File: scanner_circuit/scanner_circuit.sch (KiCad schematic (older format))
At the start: 11 parts

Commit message: Added buttons on Kicad
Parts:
- added BlueButton, GreenButton, RedButton: SW_Push_Open_Dual, symbol Switch:SW_Push_Open_Dual
- added R?: 68k, symbol Device:R
- added R? (x2): 20k, symbol Device:R
- added R?: 10k, symbol Device:R
- added R?: 100k, symbol Device:R
- added U?: dragino_lora_shield, symbol scanner_components:dragino_lora_shield
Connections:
- wire segments 41 -> 59
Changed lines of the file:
@@
-$EndComp
-$Comp
-L scanner_components:FGPMMOPA6H(gps) MOD?
-U 1 1 5DE0B476
-P 6500 3850
-F 0 "MOD?" H 6778 3896 50  0000 L CNN
-F 1 "FGPMMOPA6H(gps)" H 6778 3805 50  0000 L CNN
-F 2 "" H 6500 3950 50  0001 C CNN
-F 3 "" H 6500 3950 50  0001 C CNN
-	1    6500 3850
-	1    0    0    -1
 $EndComp
 $Comp
@@
 $EndComp
 Wire Wire Line
-	5300 3650 5900 3650
-Wire Wire Line
-	5900 3550 5300 3550
-Wire Wire Line
 	5300 3550 5300 3500
 $Comp
@@
 Wire Wire Line
 	5300 4250 5900 4250
+Wire Wire Line
+	5300 3650 5900 3650
+Wire Wire Line
+	5900 3550 5300 3550
+$Comp
+L scanner_components:FGPMMOPA6H(gps) MOD?
+U 1 1 5DE0B476
+P 6500 3850
+F 0 "MOD?" H 6778 3896 50  0000 L CNN
+F 1 "FGPMMOPA6H(gps)" H 6778 3805 50  0000 L CNN
+F 2 "" H 6500 3950 50  0001 C CNN
+F 3 "" H 6500 3950 50  0001 C CNN
+	1    6500 3850
+	1    0    0    -1
+$EndComp
+Wire Wire Line
+	8000 1950 8000 2200
+$Comp
+L power:GND #PWR?
+U 1 1 5DEF5DF5
+P 8000 2200
+F 0 "#PWR?" H 8000 1950 50  0001 C CNN
+F 1 "GND" H 8000 2050 50  0000 C CNN
+F 2 "" H 8000 2200 50  0001 C CNN
+F 3 "" H 8000 2200 50  0001 C CNN
+	1    8000 2200
+	1    0    0    -1
+$EndComp
+$Comp
+L power:+5VP #PWR?
+U 1 1 5DEFC89F
+P 7800 2200
+F 0 "#PWR?" H 7800 2050 50  0001 C CNN
+F 1 "+5VP" H 7815 2373 50  0000 C CNN
+F 2 "" H 7800 2200 50  0001 C CNN
+F 3 "" H 7800 2200 50  0001 C CNN
+	1    7800 2200
+	-1   0    0    1
+$EndComp
+Wire Wire Line
+	7800 2200 7800 1950
+$Comp
+L Device:R R?
+U 1 1 5DF037F4
+P 9800 3300
+F 0 "R?" V 9593 3300 50  0000 C CNN
+F 1 "68k" V 9684 3300 50  0000 C CNN
+F 2 "" V 9730 3300 50  0001 C CNN
+F 3 "~" H 9800 3300 50  0001 C CNN
+	1    9800 3300
+	0    1    1    0
+$EndComp
+$Comp
+L Switch:SW_Push_Open_Dual RedButton
+U 1 1 5DF02678
+P 10600 3300
+F 0 "RedButton" H 10600 3510 50  0000 C CNN
+F 1 "SW_Push_Open_Dual" H 10600 3419 50  0000 C CNN
+F 2 "" H 10600 3500 50  0001 C CNN
+F 3 "~" H 10600 3500 50  0001 C CNN
+	1    10600 3300
+	1    0    0    -1
+$EndComp
+Wire Wire Line
+	9950 3300 10400 3300
+$Comp
+L power:+5VP #PWR?
+U 1 1 5DF07955
+P 9450 3300
+F 0 "#PWR?" H 9450 3150 50  0001 C CNN
+F 1 "+5VP" H 9465 3473 50  0000 C CNN
+F 2 "" H 9450 3300 50  0001 C CNN
+F 3 "" H 9450 3300 50  0001 C CNN
+	1    9450 3300
+	0    -1   -1   0
+$EndComp
+Wire Wire Line
+	9450 3300 9650 3300
+$Comp
+L Device:R R?
+U 1 1 5DF0A509
+P 9800 4150
+F 0 "R?" V 9593 4150 50  0000 C CNN
+F 1 "20k" V 9684 4150 50  0000 C CNN
+F 2 "" V 9730 4150 50  0001 C CNN
+F 3 "~" H 9800 4150 50  0001 C CNN
+	1    9800 4150
+	0    1    1    0
+$EndComp
+$Comp
+L Switch:SW_Push_Open_Dual BlueButton
+U 1 1 5DF0A50F
+P 10600 4150
+F 0 "BlueButton" H 10600 4360 50  0000 C CNN
+F 1 "SW_Push_Open_Dual" H 10600 4269 50  0000 C CNN
+F 2 "" H 10600 4350 50  0001 C CNN
+F 3 "~" H 10600 4350 50  0001 C CNN
+	1    10600 4150
+	1    0    0    -1
+$EndComp
+Wire Wire Line
+	9950 4150 10400 4150
+$Comp
+L power:+5VP #PWR?
+U 1 1 5DF0A516
+P 9450 4150
+F 0 "#PWR?" H 9450 4000 50  0001 C CNN
+F 1 "+5VP" H 9465 4323 50  0000 C CNN
+F 2 "" H 9450 4150 50  0001 C CNN
+F 3 "" H 9450 4150 50  0001 C CNN
+	1    9450 4150
+	0    -1   -1   0
+$EndComp
+Wire Wire Line
+	9450 4150 9650 4150
+$Comp
+L Device:R R?
+U 1 1 5DF0D043
+P 9450 5000
+F 0 "R?" V 9243 5000 50  0000 C CNN
+F 1 "10k" V 9334 5000 50  0000 C CNN
+F 2 "" V 9380 5000 50  0001 C CNN
+F 3 "~" H 9450 5000 50  0001 C CNN
+	1    9450 5000
+	0    1    1    0
+$EndComp
+$Comp
+L Switch:SW_Push_Open_Dual GreenButton
+U 1 1 5DF0D049
+P 10600 5000
+F 0 "GreenButton" H 10600 5210 50  0000 C CNN
+F 1 "SW_Push_Open_Dual" H 10600 5119 50  0000 C CNN
+F 2 "" H 10600 5200 50  0001 C CNN
+F 3 "~" H 10600 5200 50  0001 C CNN
+	1    10600 5000
+	1    0    0    -1
+$EndComp
+$Comp
+L power:+5VP #PWR?
+U 1 1 5DF0D050
+P 9100 5000
+F 0 "#PWR?" H 9100 4850 50  0001 C CNN
+F 1 "+5VP" H 9115 5173 50  0000 C CNN
+F 2 "" H 9100 5000 50  0001 C CNN
+F 3 "" H 9100 5000 50  0001 C CNN
+	1    9100 5000
+	0    -1   -1   0
+$EndComp
+Wire Wire Line
+	9100 5000 9300 5000
+$Comp
+L scanner_components:dragino_lora_shield U?
+U 1 1 5DEF3113
+P 7000 2100
+F 0 "U?" H 8878 2771 50  0000 L CNN
+F 1 "dragino_lora_shield" H 8878 2680 50  0000 L CNN
+F 2 "" H 7000 2850 50  0001 C CNN
+F 3 "" H 7000 2850 50  0001 C CNN
+	1    7000 2100
+	1    0    0    -1
+$EndComp
+Wire Wire Line
+	8700 1950 8700 2650
+Wire Wire Line
+	8700 3500 10400 3500
+Wire Wire Line
+	10400 4350 8700 4350
+Wire Wire Line
+	8700 4350 8700 3500
+Connection ~ 8700 3500
+Wire Wire Line
+	10400 5200 8700 5200
+Wire Wire Line
+	8700 5200 8700 4350
+Connection ~ 8700 4350
+Wire Wire Line
+	8700 2650 9100 2650
+Connection ~ 8700 2650
+Wire Wire Line
+	8700 2650 8700 3500
+$Comp
+L Device:R R?
+U 1 1 5DF1893C
+P 9250 2650
+F 0 "R?" V 9043 2650 50  0000 C CNN
+F 1 "100k" V 9134 2650 50  0000 C CNN
+F 2 "" V 9180 2650 50  0001 C CNN
+F 3 "~" H 9250 2650 50  0001 C CNN
+	1    9250 2650
+	0    1    1    0
+$EndComp
+Wire Wire Line
+	9400 2650 10050 2650
+$Comp
+L power:GND #PWR?
+U 1 1 5DF1B53E
+P 10050 2650
+F 0 "#PWR?" H 10050 2400 50  0001 C CNN
+F 1 "GND" H 10055 2477 50  0000 C CNN
+F 2 "" H 10050 2650 50  0001 C CNN
+F 3 "" H 10050 2650 50  0001 C CNN
+	1    10050 2650
+	0    -1   -1   0
+$EndComp
+Wire Wire Line
+	9600 5000 9800 5000
+$Comp
+L Device:R R?
+U 1 1 5DF20956
+P 9950 5000
+F 0 "R?" V 9743 5000 50  0000 C CNN
+F 1 "20k" V 9834 5000 50  0000 C CNN
+F 2 "" V 9880 5000 50  0001 C CNN
+F 3 "~" H 9950 5000 50  0001 C CNN
+	1    9950 5000
+	0    1    1    0
+$EndComp
+Wire Wire Line
+	10100 5000 10400 5000
 $EndSCHEMATC

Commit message: Working on schematic for TTN Mapper
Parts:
- removed BlueButton, GreenButton, RedButton: SW_Push_Open_Dual, symbol Switch:SW_Push_Open_Dual
- added SW?: Red_Button, symbol Switch:SW_Push
- added SW?: Blue_Button, symbol Switch:SW_Push
- added SW?: Green_Button, symbol Switch:SW_Push
- MOD?: value FGPMMOPA6H(gps) -> GPS MODUL - FGPMMOPA6H
- U?: value dragino_lora_shield -> LoRa Shield
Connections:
- net labels added: A0, A1
- wire segments 59 -> 62
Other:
- moved on the sheet: C?, MOD?, Q?, R?, U?

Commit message: Worked further on TTN mapper and fixed a bug in main file
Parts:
- added C6, C8: 100nF, symbol Device:C_Small
- added C7, C9: 10uF, symbol Device:CP_Small
- added DS1: LCD Screen, Display:WC1602A, symbol Display_Character:WC1602A
- added R10, R11, R13: 120R, symbol Device:R
- added R12: 620R, symbol Device:R
- added R4: 220R, symbol Device:R_Small
- added RV1: 10K_Potentiometer, symbol Device:R_POT
- added U3: LD1117S33TR_SOT223, Package_TO_SOT_SMD:SOT-223-3_TabPin2, symbol Regulator_Linear:LD1117S33TR_SOT223
- added U4: LM317_TO220, Package_TO_SOT_THT:TO-220-3_Vertical, symbol Regulator_Linear:LM337_TO220
- MOD1: renamed from MOD?; value GPS MODUL - FGPMMOPA6H -> GPS MODULE
- gave numbers to parts that had none: 19
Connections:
- net UNO_RX is gone; now on net D3: U1.5 (PD3)
- net +3V3: now also C7.1, U3.2 (VO)
- net +5VP: now also C9.1, DS1.2 (VDD), R10.2, R4.2, RV1.1, U4.3 (VO)
- net A1: now also U2.31 (1)
- net GND: now also U2.24 (GND), U2.25 (GND), C6.2, C7.2, C8.2, C9.2, DS1.1 (VSS), DS1.16 (LED(-)), DS1.5 (R/W), R13.1, RV1.3, U3.1 (GND)
- net D5: now reaches U1.11 (PD5)
- net D5: now also U2.6 (5), DS1.11 (D4)
- net D6: now reaches U1.12 (PD6)
- net D6: now also U2.7 (6)
- net D7: now reaches U1.13 (PD7)
- net D7: now also U2.8 (7)
- net D8: now reaches U1.14 (PB0)
- net D8: now also U2.9 (8)
- net D9: now reaches U1.15 (PB1)
- net D9: now also U2.10 (9)
- net D10: now reaches U1.16 (PB2)
- net D10: now also U2.11 (10)
- net D11: now reaches U1.17 (PB3)
- net D11: now also U2.12 (11)
- net D12: now reaches U1.18 (PB4)
- net D12: now also U2.13 (12)
- net D13: now reaches U1.19 (PB5)
- net D13: now also U2.14 (13)
- net RX: now reaches U1.2 (PD0)
- net RX: now also U2.2 (1)
- net AREF: now reaches U1.21 (AREF)
- net AREF: now also U2.16 (AREF)
- net A2: now reaches U1.25 (PC2)
- net A2: now also U2.30 (2)
- net A3: now reaches U1.26 (PC3)
- net A3: now also U2.29 (3), DS1.14 (D7)
- net A4: now reaches U1.27 (PC4)
- net A4: now also U2.17 (SDA), U2.28 (4), DS1.6 (E)
- net A5: now reaches U1.28 (PC5)
- net A5: now also U2.18 (SCL), U2.27 (5), DS1.4 (RS)
- net TX: now reaches U1.3 (PD1)
- net TX: now also U2.1 (0)
- net D2: now reaches U1.4 (PD2)
- net D2: now also U2.3 (2)
- net D4: now reaches U1.6 (PD4)
- net D4: now also U2.5 (4), DS1.12 (D5)
- net D3: now reaches U2.4 (3)
- net D3: now also DS1.13 (D6)
- new net: DS1.15 (LED(+)), R4.1
- new net: DS1.3 (VO), RV1.2
- new net: R11.1, R12.2, U4.1 (ADJ)
- new net: C8.1, U4.2 (VI)
- new net: C6.1, U3.3 (VI)
- new net: R10.1, R11.2
- new net: R12.1, R13.2
- no-connect marks 0 -> 12
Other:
- moved on the sheet: C1, C2, C3, C4, Q1, R1, R2, R3, R5, R6, R7, R8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

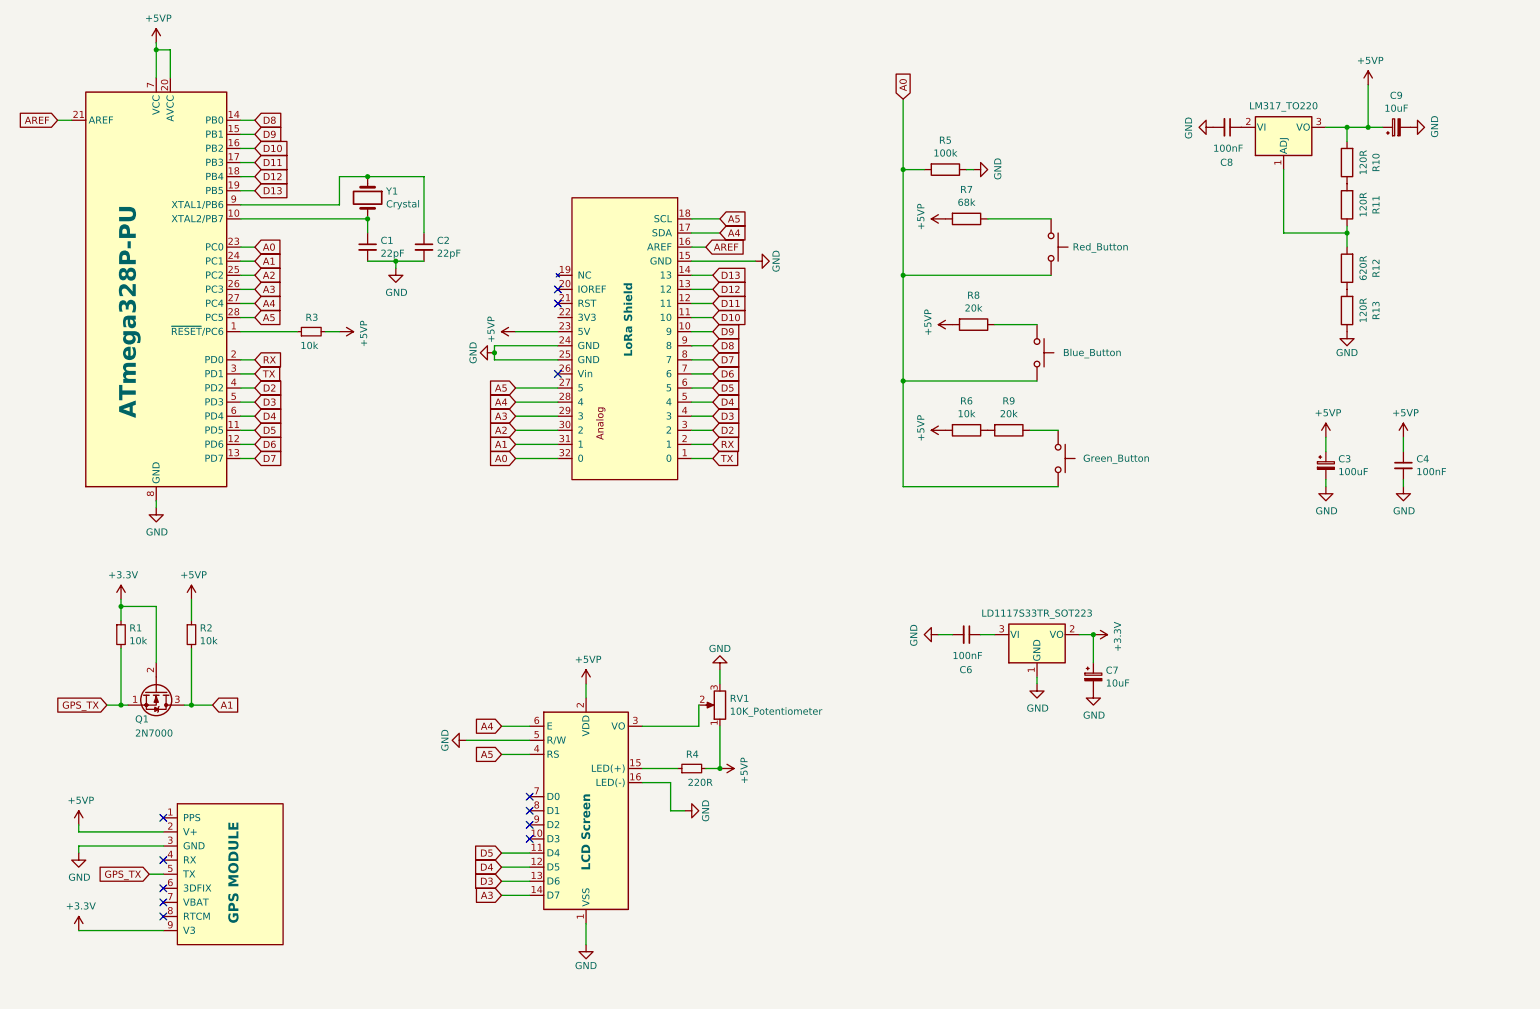
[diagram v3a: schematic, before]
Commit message: Cleanup of TTN Mapper schematic
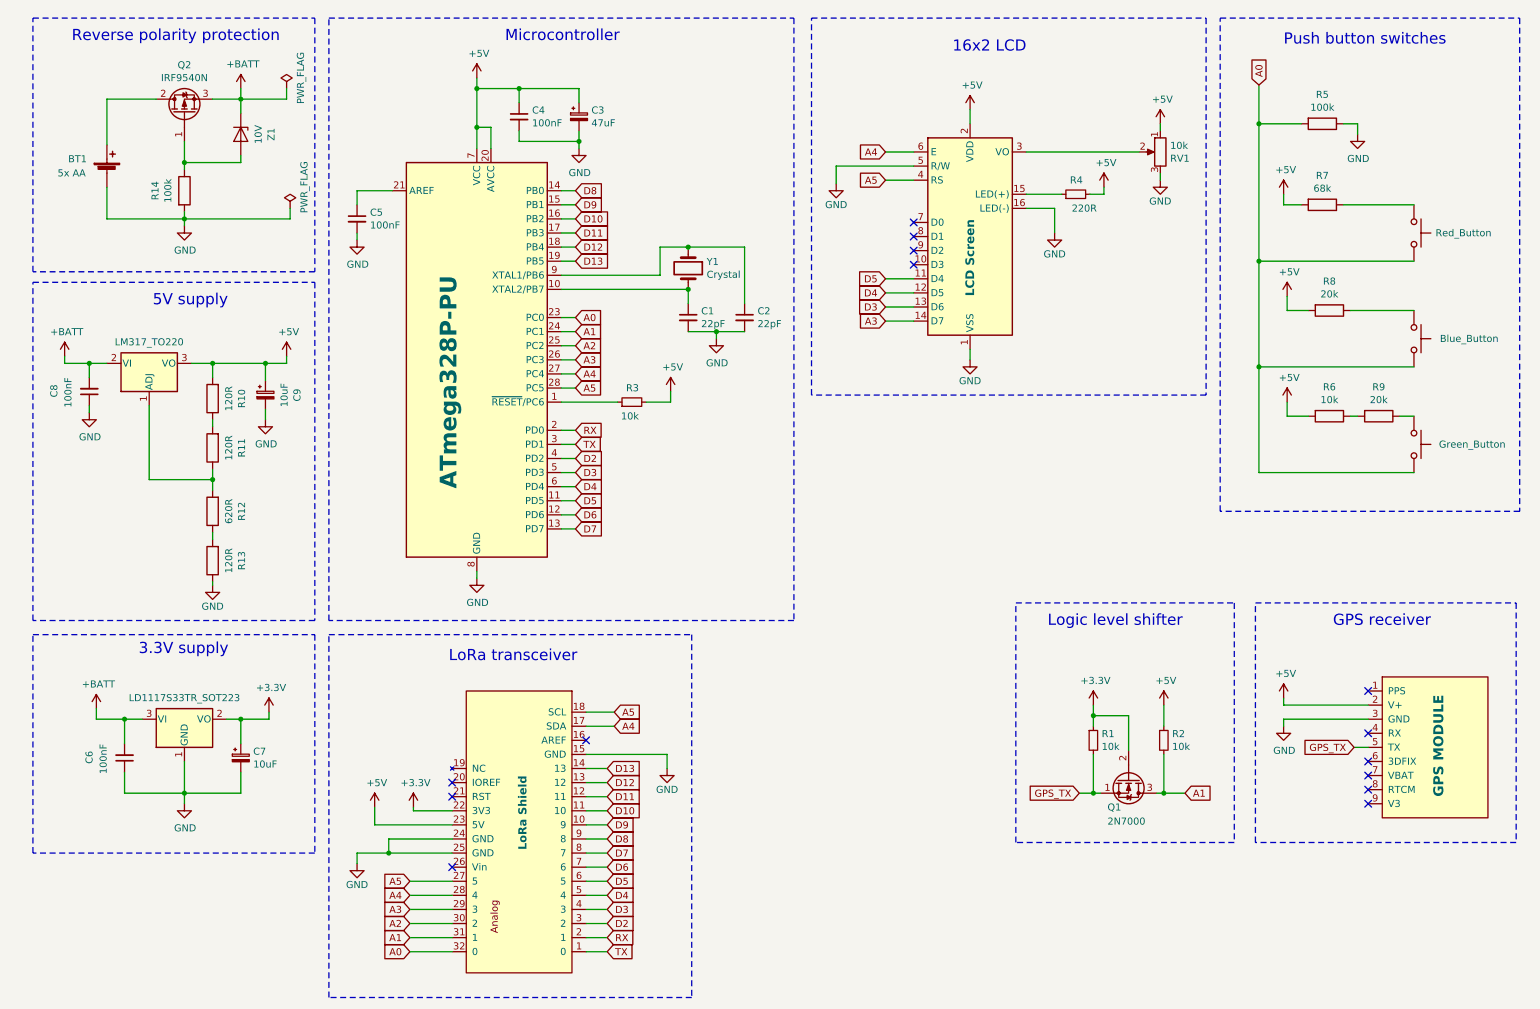
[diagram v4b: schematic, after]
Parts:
- added BT1: 5x AA, symbol Device:Battery_Cell
- added C5: 100nF, symbol Device:C_Small
- added Q2: IRF9540N, Package_TO_SOT_THT:TO-220-3_Vertical, symbol Transistor_FET:IRF9540N
- added R14: 100k, symbol Device:R
- added Z1: 10V, Diode_THT:D_DO-41_SOD81_P10.16mm_Horizontal, symbol Diode:ZPYxx
- C3: value 100uF -> 47uF
- RV1: value 10K_Potentiometer -> 10k
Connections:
- net +3V3: now also U2.22 (3V3); no longer MOD1.9 (V3)
- net GND: now also C6.1, C8.1, BT1.2 (-), C5.2, R14.2; no longer C6.2, C8.2
- net +BATT: now reaches U4.2 (VI)
- net +BATT: now also C6.2, C8.2, U3.3 (VI), Q2.3 (S), Z1.1 (K); no longer C8.1
- net +5VP renamed +5V
- net AREF: no longer names the net of U1.21 (AREF)
- net AREF: now also C5.1; no longer U2.16 (AREF)
- new net: Q2.1 (G), R14.1, Z1.2 (A)
- new net: BT1.1 (+), Q2.2 (D)
- no-connect marks 12 -> 14
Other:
- note added: "16x2 LCD"
- note added: "3.3V supply"
- note added: "5V supply"
- note added: "GPS receiver"
- note added: "LoRa transceiver"
- note added: "Logic level shifter"
- note added: "Microcontroller"
- note added: "Push button switches"
- note added: "Reverse polarity protection"
- moved on the sheet: C1, C2, C3, C4, C6, C7, C8, C9, Q1, R1, R10, R11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

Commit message: Added programming header to TTN Mapper
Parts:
- added J?: AVR-ISP-6, symbol Connector:AVR-ISP-6
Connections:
- net +5V: now also J?.2 (VCC)
- net D11: now also J?.4 (MOSI)
- net D12: now also J?.1 (MISO)
- net D13: now also J?.3 (SCK)
- net GND: now also J?.6 (GND)
- net RESET: now reaches R3.1, U1.1 (~RESET~/PC6)
- net RESET: now also J?.5 (~RST)
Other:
- note added: "Programming header"
- moved on the sheet: Q1, R1, R2, R3
